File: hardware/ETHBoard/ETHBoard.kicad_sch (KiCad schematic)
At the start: 24 parts, among them J1 Conn_02x04_Odd_Even, J2 Conn_01x02_Pin, U1 LAN8651B1-E_LMX, Y1 X322525MOB4SI

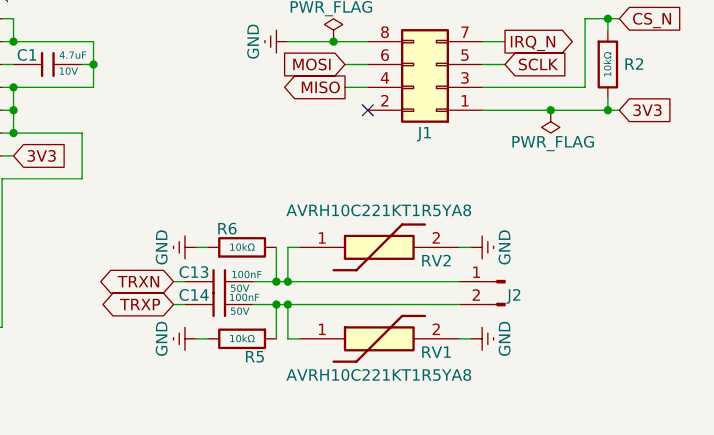
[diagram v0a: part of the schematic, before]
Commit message: Minor ETHBoard tweaks.
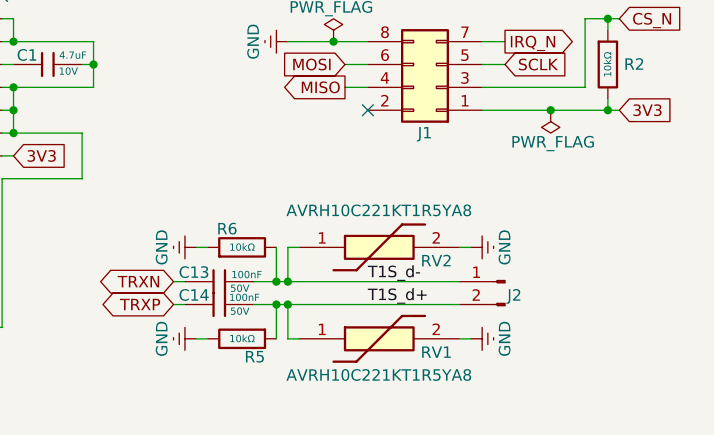
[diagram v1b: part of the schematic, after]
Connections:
- net T1S_d+: now reaches C14.2, J2.2 (Pin_2), R5.1, RV1.1
- net T1S_d-: now reaches C13.2, J2.1 (Pin_1), R6.2, RV2.1
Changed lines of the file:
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@@
+		)
+	)
+	(label "T1S_d+"
+		(at 104.14 99.06 0)
+		(effects
+			(font
+				(size 1.27 1.27)
+			)
+			(justify left bottom)
+		)
+	)
+	(label "T1S_d-"
+		(at 104.14 96.52 0)
+		(effects
+			(font
+				(size 1.27 1.27)
+			)
+			(justify left bottom)
 		)
 	)

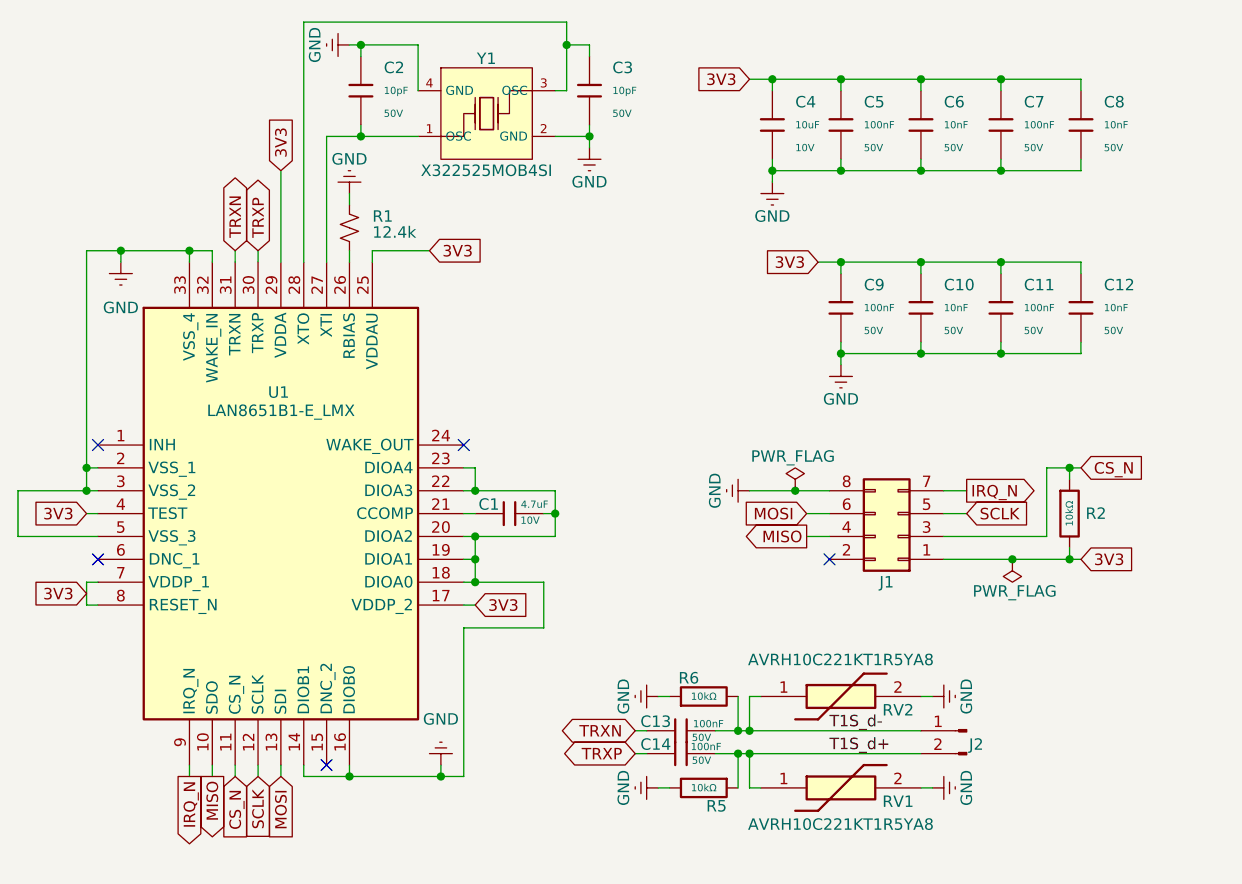
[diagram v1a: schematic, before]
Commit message: Reverted back to using std lib (not jlcpcb).
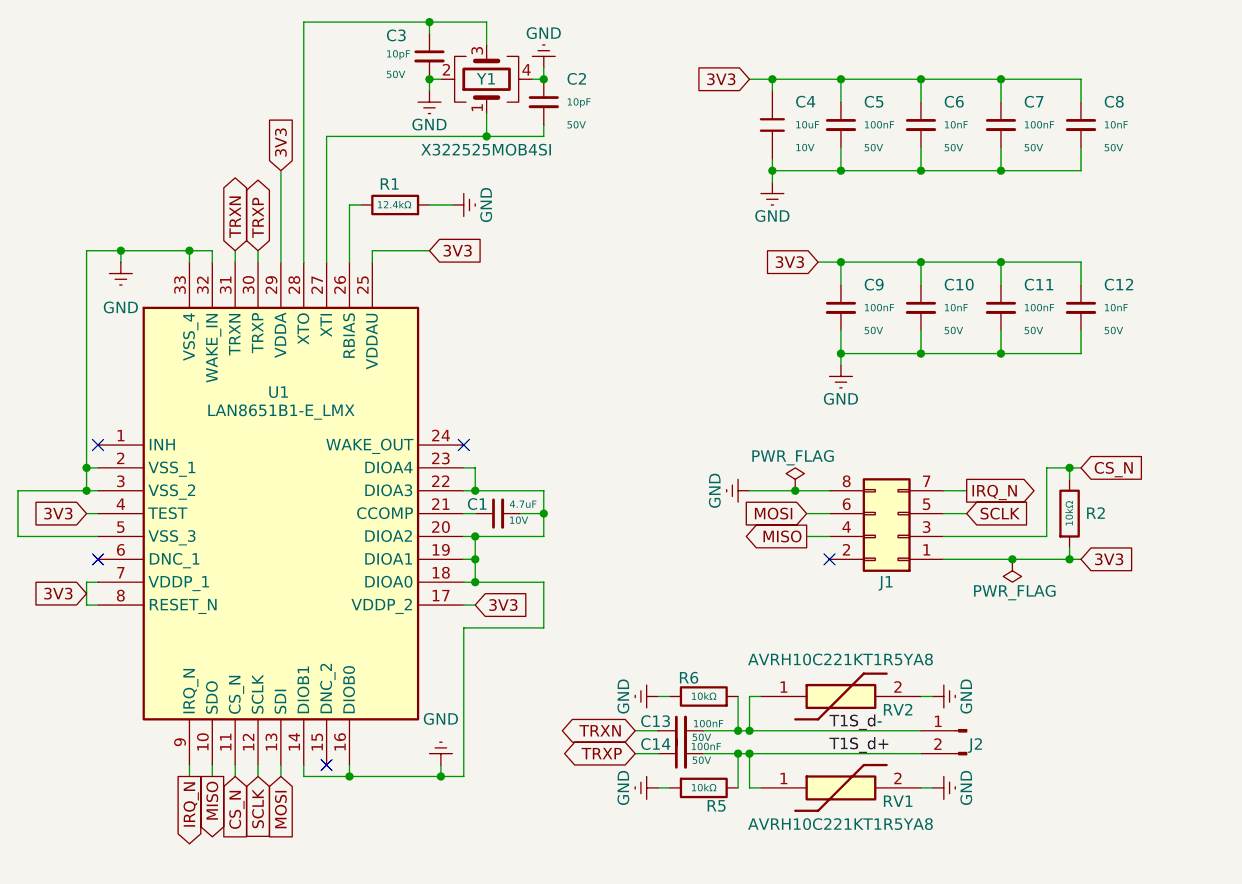
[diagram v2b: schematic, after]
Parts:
- C1: footprint PCM_JLCPCB:C_0402 -> Capacitor_SMD:C_0402_1005Metric; symbol PCM_JLCPCB-Capacitors:0402,4.7uF -> Device:C_Small
- C10, C12, C6, C8: footprint PCM_JLCPCB:C_0402 -> Capacitor_SMD:C_0402_1005Metric; symbol PCM_JLCPCB-Capacitors:0402,10nF -> Device:C_Small
- C11, C13, C14, C5, C7, C9: footprint PCM_JLCPCB:C_0402 -> Capacitor_SMD:C_0402_1005Metric; symbol PCM_JLCPCB-Capacitors:0402,100nF,(2) -> Device:C_Small
- C2, C3: footprint PCM_JLCPCB:C_0402 -> Capacitor_SMD:C_0402_1005Metric; symbol PCM_JLCPCB-Capacitors:0402,10pF -> Device:C_Small
- C4: footprint PCM_JLCPCB:C_0603 -> Capacitor_SMD:C_0603_1608Metric
- J1, J2: now left out of the parts list
- R1: value 12.4k -> 12.4kΩ; footprint PCM_SparkFun-Resistor:R_0603_1608Metric -> Resistor_SMD:R_0603_1608Metric; symbol PCM_SparkFun-Resistor:12.4k_0603 -> Device:R
- R2: footprint PCM_JLCPCB:R_0603 -> Resistor_SMD:R_0603_1608Metric; symbol PCM_JLCPCB-Resistors:0603,10kΩ -> Device:R
- R5, R6: footprint PCM_JLCPCB:R_1206 -> Resistor_SMD:R_1206_3216Metric; symbol PCM_JLCPCB-Resistors:1206,10kΩ -> Device:R
- Y1: footprint PCM_JLCPCB:OSC-SMD_4P-L3.2-W2.5-BL -> Crystal:Crystal_SMD_3225-4Pin_3.2x2.5mm; symbol PCM_JLCPCB-Crystals:Crystal, 25MHz, 11pF -> Device:Crystal_GND24
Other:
- moved on the sheet: C1, C2, C3

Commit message: More cleanup, pipline should run now.
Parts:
- C4: symbol PCM_JLCPCB-Capacitors:0603,10uF -> Device:C_Small
- R2: Overload Voltage (Max) 75V -> (none); Overload Voltage Max (none) -> 75V; Power (none) -> 100mW; Power(Watts) 100mW -> (none)
- R5, R6: Overload Voltage (Max) 200V -> (none); Overload Voltage Max (none) -> 200V; Power (none) -> 250mW; Power(Watts) 250mW -> (none)
- RV1, RV2: Mouser Price Stock (none) -> https://www.mouser.co.uk/ProductDetail/TDK/AVRH10C221KT1R5Y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; Mouser Price/Stock https://www.mouser.co.uk/ProductDetail/TDK/AVRH10C221KT1R5Y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 -> (none)
- U1: Mouser Price Stock (none) -> https://www.mouser.co.uk/ProductDetail/Microchip-Technology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; Mouser Price/Stock https://www.mouser.co.uk/ProductDetail/Microchip-Technology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 -> (none)
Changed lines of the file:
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@@
 	(wire
 		(pts
-			(xy 97.79 33.02) (xy 97.79 34.29)
+			(xy 97.79 31.75) (xy 97.79 34.29)
 		)
 		(stroke
@@
 	(wire
 		(pts
-			(xy 97.79 24.13) (xy 97.79 25.4)
+			(xy 38.1 43.18) (xy 38.1 44.45)
 		)
 		(stroke
@@
 	(wire
 		(pts
-			(xy 38.1 43.18) (xy 38.1 44.45)
+			(xy 114.3 24.13) (xy 123.19 24.13)
 		)
 		(stroke
@@
 	(wire
 		(pts
-			(xy 114.3 24.13) (xy 123.19 24.13)
+			(xy 53.34 43.18) (xy 53.34 44.45)
 		)
 		(stroke
@@
 	(wire
 		(pts
-			(xy 53.34 43.18) (xy 53.34 44.45)
+			(xy 116.84 74.93) (xy 128.27 74.93)
 		)
 		(stroke
@@
 	(wire
 		(pts
-			(xy 116.84 74.93) (xy 128.27 74.93)
+			(xy 72.39 72.39) (xy 72.39 74.93)
 		)
 		(stroke
@@
 	(wire
 		(pts
-			(xy 72.39 72.39) (xy 72.39 74.93)
+			(xy 97.79 24.13) (xy 97.79 26.67)
 		)
 		(stroke
@@
 			)
 		)
-		(property "Power(Watts)" "250mW"
+		(property "Power" "250mW"
 			(at 90.17 102.87 0)
 			(effects
@@
 			)
 		)
-		(property "Overload Voltage (Max)" "200V"
+		(property "Overload Voltage Max" "200V"
 			(at 90.17 102.87 0)
 			(effects
@@
 	)
 	(symbol
-		(lib_id "PCM_JLCPCB-Capacitors:0603,10uF")
+		(lib_id "Device:C_Small")
 		(at 97.79 29.21 0)
 		(unit 1)
@@
 		(fields_autoplaced yes)
 		(property "Reference" "C4"
-			(at 100.33 26.6699 0)
+			(at 100.33 26.6762 0)
 			(effects
 				(font
@@
 		)
 		(property "Value" "10uF"
-			(at 100.33 29.21 0)
+			(at 100.33 29.2163 0)
 			(effects
 				(font
@@
 		)
 		(property "Footprint" "Capacitor_SMD:C_0603_1608Metric"
-			(at 96.012 29.21 90)
+			(at 97.79 29.21 0)
 			(effects
 				(font
@@
 			)
 		)
-		(property "Datasheet" "https://www.lcsc.com/datasheet/lcsc_datasheet_2304140030_Samsung-Electro-Mechanics-CL10A106KP8NNNC_C19702.pdf"
+		(property "Datasheet" "~"
 			(at 97.79 29.21 0)
 			(effects
@@
 			)
 		)
-		(property "Description" "10V 10uF X5R ±10% 0603 Multilayer Ceramic Capacitors MLCC - SMD/SMT ROHS"
+		(property "Description" "Unpolarized capacitor, small symbol"
 			(at 97.79 29.21 0)
 			(effects
@@
 		)
 		(property "Voltage Rated" "10V"
-			(at 100.33 31.75 0)
+			(at 100.33 31.7563 0)
 			(effects
 				(font
@@
 			)
 		)
-		(property "Power(Watts)" "250mW"
+		(property "Power" "250mW"
 			(at 90.17 92.71 0)
 			(effects
@@
 			)
 		)
-		(property "Overload Voltage (Max)" "200V"
+		(property "Overload Voltage Max" "200V"
 			(at 90.17 92.71 0)
 			(effects
@@
 			)
 		)
-		(property "Mouser Price/Stock" "https://www.mouser.co.uk/ProductDetail/TDK/AVRH10C221KT1R5YA8?qs=P1JMDcb91o7%2FqB%252BLJliAkA%3D%3D"
+		(property "Mouser Price Stock" "https://www.mouser.co.uk/ProductDetail/TDK/AVRH10C221KT1R5YA8?qs=P1JMDcb91o7%2FqB%252BLJliAkA%3D%3D"
 			(at 110.49 699.06 0)
 			(effects
@@
 			)
 		)
-		(property "Mouser Price/Stock" "https://www.mouser.co.uk/ProductDetail/Microchip-Technology/LAN8651B1-E-LMX?qs=HoCaDK9Nz5cTGz8XEJbodA%3D%3D"
+		(property "Mouser Price Stock" "https://www.mouser.co.uk/ProductDetail/Microchip-Technology/LAN8651B1-E-LMX?qs=HoCaDK9Nz5cTGz8XEJbodA%3D%3D"
 			(at 59.69 846.99 0)
 			(effects
@@
 			)
 		)
-		(property "Arrow Price/Stock" ""
+		(property "Arrow Price Stock" ""
 			(at 59.69 1046.99 0)
 			(effects
@@
 			)
 		)
-		(property "Mouser Price/Stock" "https://www.mouser.co.uk/ProductDetail/TDK/AVRH10C221KT1R5YA8?qs=P1JMDcb91o7%2FqB%252BLJliAkA%3D%3D"
+		(property "Mouser Price Stock" "https://www.mouser.co.uk/ProductDetail/TDK/AVRH10C221KT1R5YA8?qs=P1JMDcb91o7%2FqB%252BLJliAkA%3D%3D"
 			(at 110.49 688.9 0)
 			(effects
@@
 			)
 		)
-		(property "Power(Watts)" "100mW"
+		(property "Power" "100mW"
 			(at 130.81 72.39 0)
 			(effects
@@
 			)
 		)
-		(property "Overload Voltage (Max)" "75V"
+		(property "Overload Voltage Max" "75V"
 			(at 130.81 72.39 0)
 			(effects

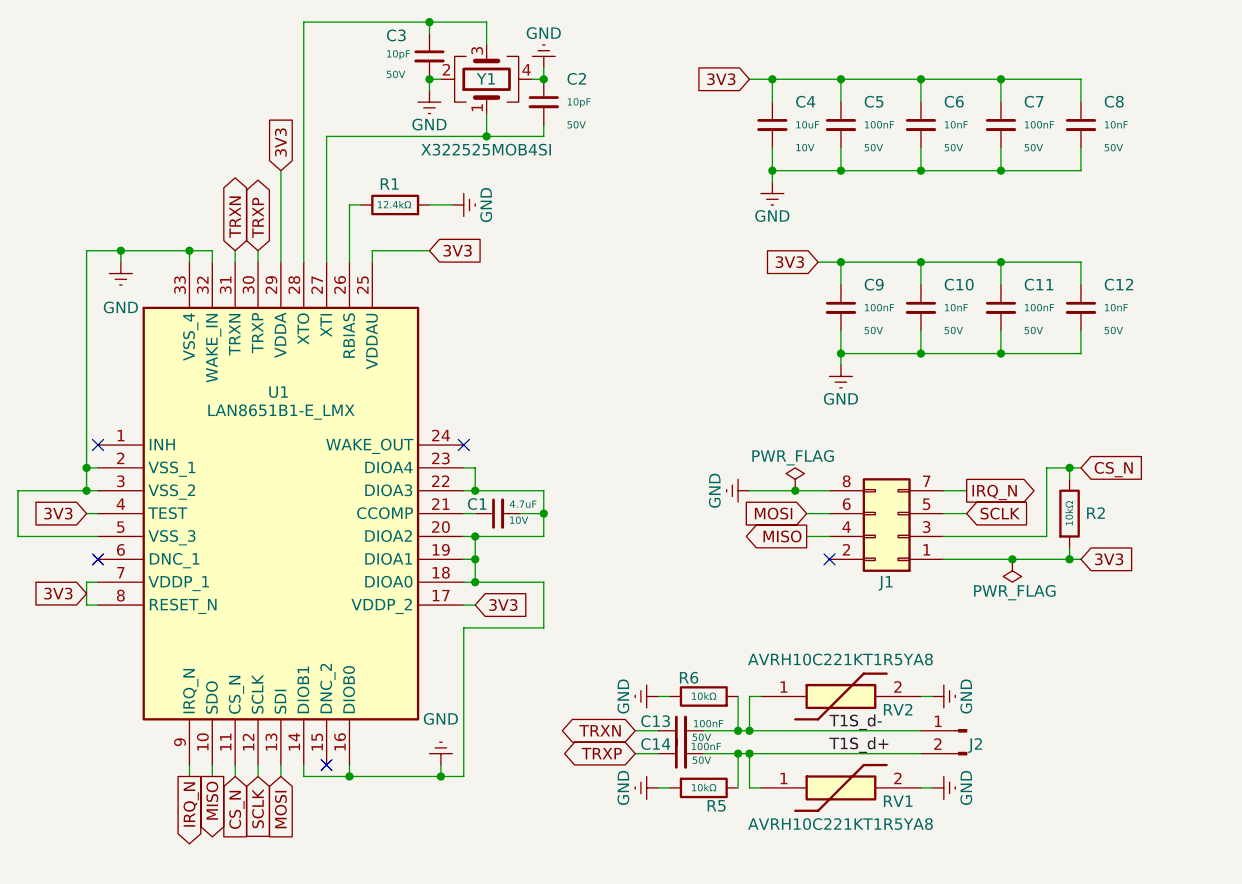
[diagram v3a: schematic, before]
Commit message: Rework ETHBoard.
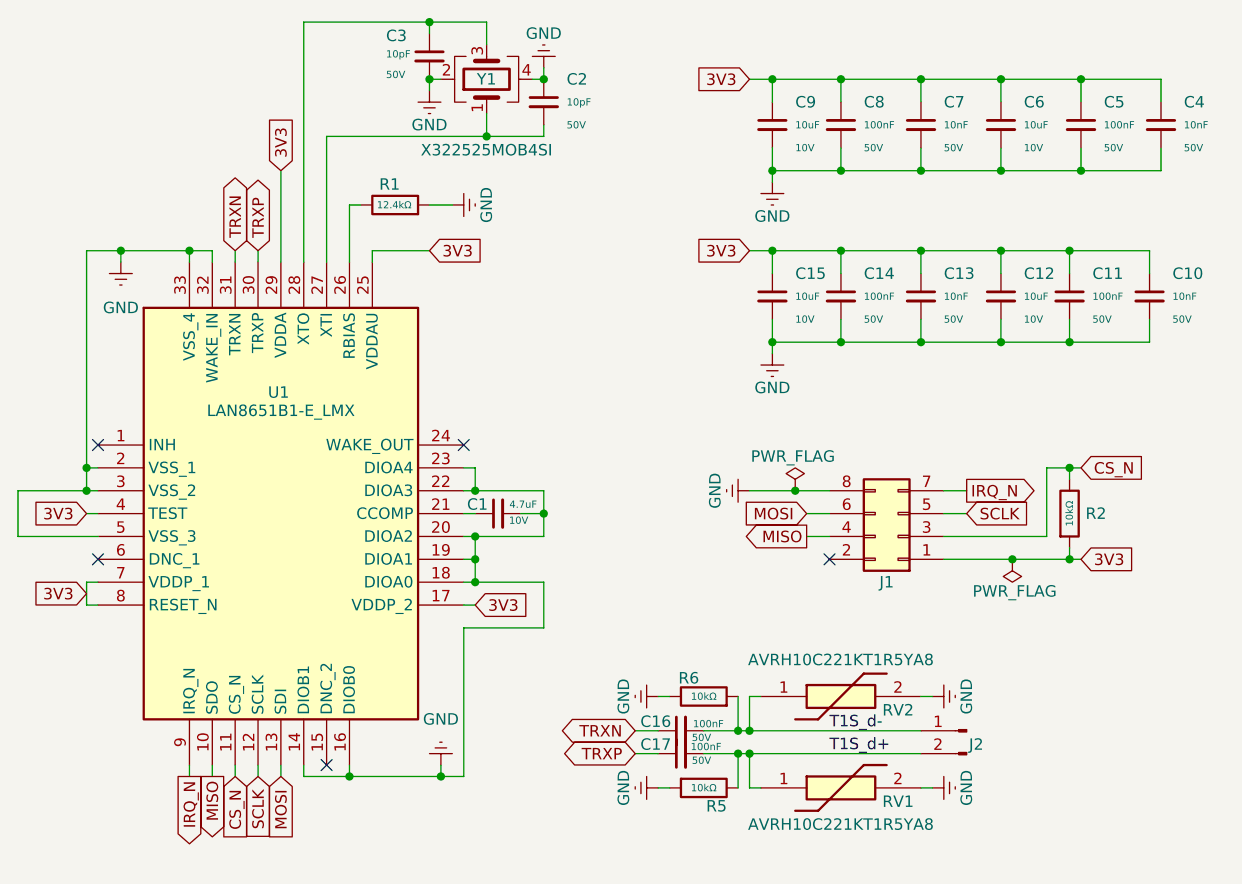
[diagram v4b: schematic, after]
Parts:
- added C12, C15, C6: 10uF, Capacitor_SMD:C_0402_1005Metric, symbol Device:C_Small
- C1: footprint Capacitor_SMD:C_0402_1005Metric -> Capacitor_SMD:C_0603_1608Metric
- C16: renamed from C13; footprint Capacitor_SMD:C_0402_1005Metric -> Capacitor_SMD:C_0805_2012Metric
- C17: renamed from C14; footprint Capacitor_SMD:C_0402_1005Metric -> Capacitor_SMD:C_0805_2012Metric
- C9: renamed from C4; footprint Capacitor_SMD:C_0603_1608Metric -> Capacitor_SMD:C_0402_1005Metric
- R1, R2: footprint Resistor_SMD:R_0603_1608Metric -> Resistor_SMD:R_0402_1005Metric
- renumbered C12 to C10, C10 to C13, C9 to C14, C8 to C4, C7 to C5, C6 to C7, C5 to C8
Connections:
- net 3V3: now also C12.1, C15.1, C6.1
- net GND: now also C12.2, C15.2, C6.2
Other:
- moved on the sheet: C10, C11, C13, C14, C4, C5

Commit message: Added common mode choke.
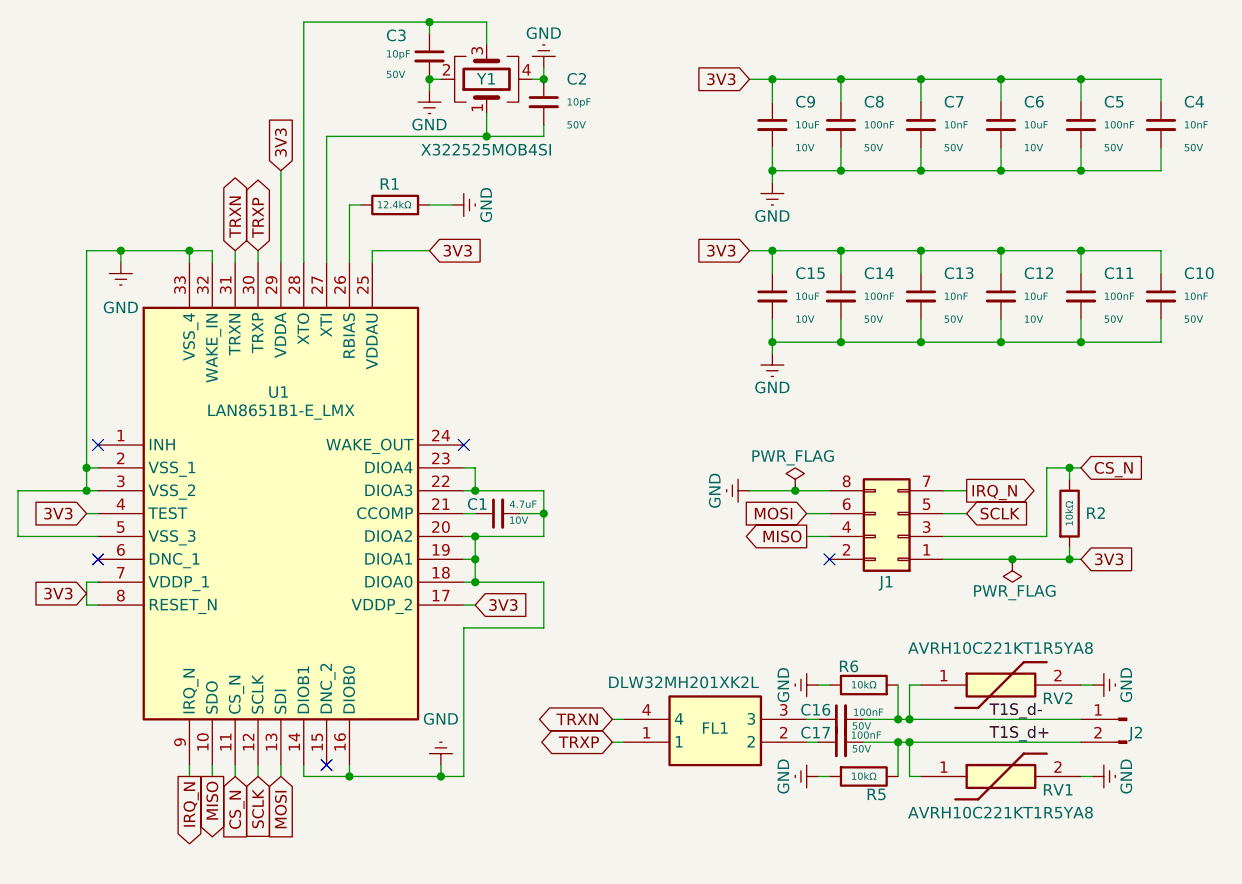
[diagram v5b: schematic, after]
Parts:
- added FL1: DLW32MH201XK2L, LIB_DLW32MH201XK2L:DLW32MH101XK2L, symbol DLW32MH201XK2L:DLW32MH201XK2L
- C16, C17: footprint Capacitor_SMD:C_0805_2012Metric -> Capacitor_SMD:C_0603_1608Metric
- RV1, RV2: Mouser Price/Stock (none) -> https://www.mouser.co.uk/ProductDetail/TDK/AVRH10C221KT1R5Y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
- U1: Mouser Price/Stock (none) -> https://www.mouser.co.uk/ProductDetail/Microchip-Technology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
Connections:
- net TRXN: now also FL1.4; no longer C16.1
- net TRXP: now also FL1.1; no longer C17.1
- new net: C17.1, FL1.2
- new net: C16.1, FL1.3
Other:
- moved on the sheet: C10, C11, C16, C17, J2, R5, R6, RV1, RV2

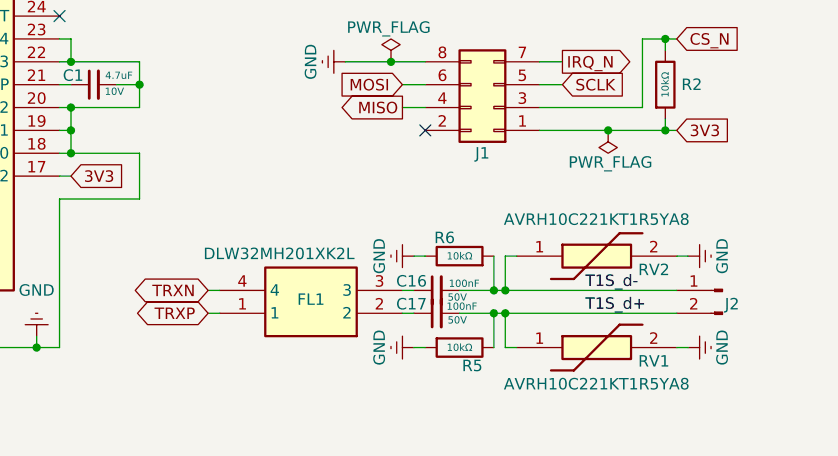
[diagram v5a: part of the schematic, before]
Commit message: Added termination parts for ETHBoard.
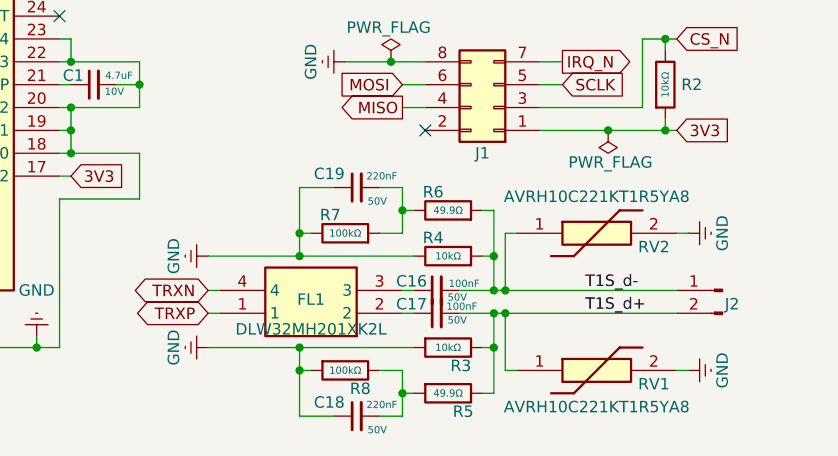
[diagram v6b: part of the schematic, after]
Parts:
- added C18, C19: 220nF, Capacitor_SMD:C_0805_2012Metric, symbol Device:C_Small
- added R5, R6: 49.9Ω, Resistor_SMD:R_1206_3216Metric, symbol Device:R
- added R7, R8: 100kΩ, Resistor_SMD:R_1206_3216Metric, symbol Device:R
- renumbered R5 to R3, R6 to R4
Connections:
- net GND: now also C18.1, C19.1, R7.1, R8.2
- net T1S_d+: now also R5.1
- net T1S_d-: now also R6.2
- new net: C19.2, R6.1, R7.2
- new net: C18.2, R5.2, R8.1
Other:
- moved on the sheet: R3, R4, RV1, RV2
